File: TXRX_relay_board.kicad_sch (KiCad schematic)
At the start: 76 parts, among them J1 Screw_Terminal_01x02, J2 Conn_01x08, J3 IN, J4 IN_RF_Deck, J5 OUT_RF_Deck, J6 OUT, K1 RT314A05, K2 RT314A05, Q1 MMSS8550HE3, Q2 MMSS8550HE3, Q3 BC847, Q4 PNP, Q5 MMSS8550HE3, Q6 PNP, U1 OP07, U2 AMS1117-5.0

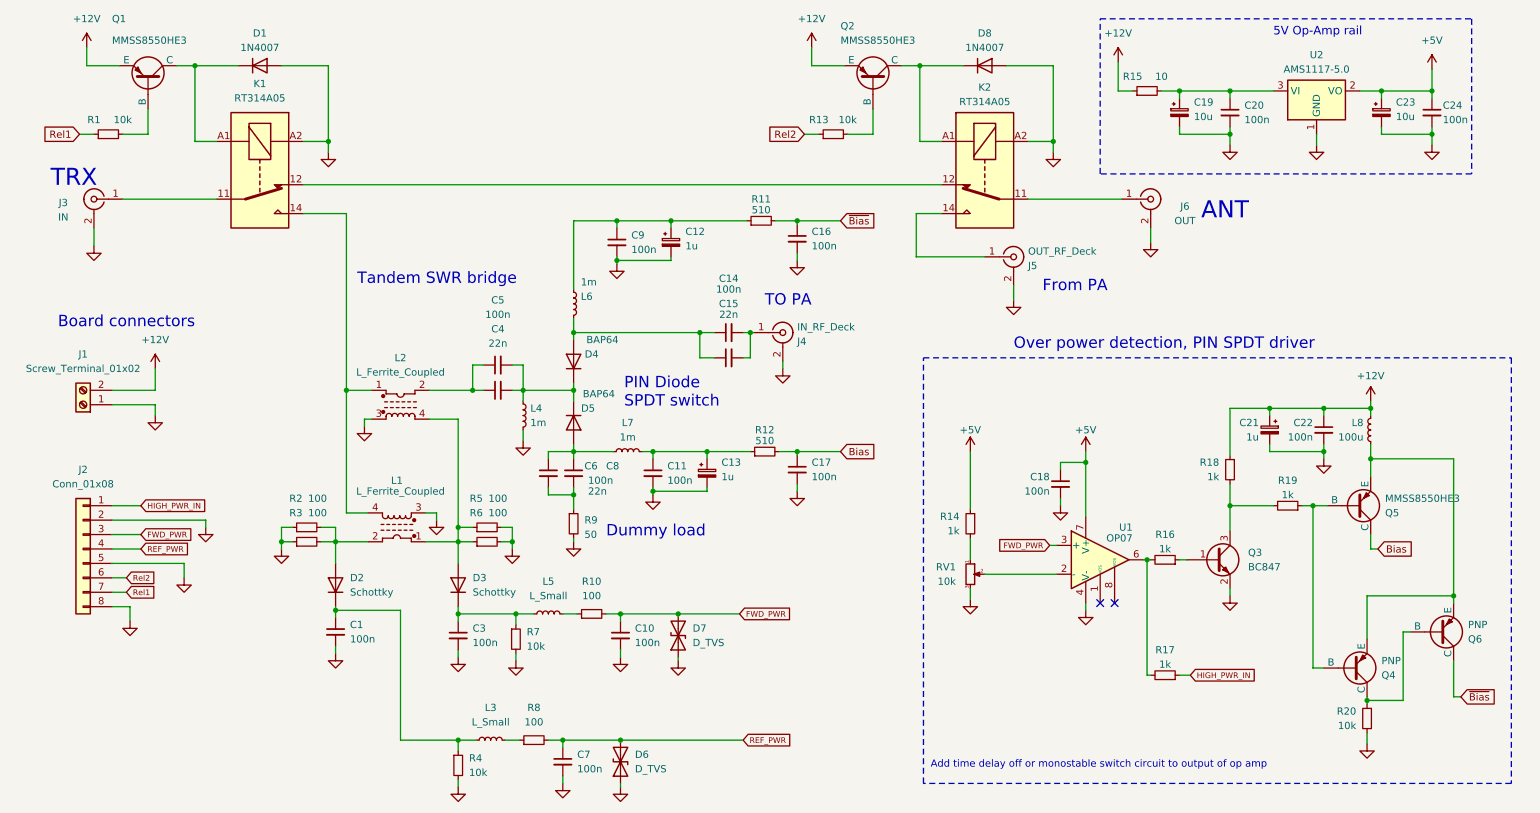
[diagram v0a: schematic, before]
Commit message: rev 1.2
Minor fixes, coupler measurements, falstad simulation of over power protection
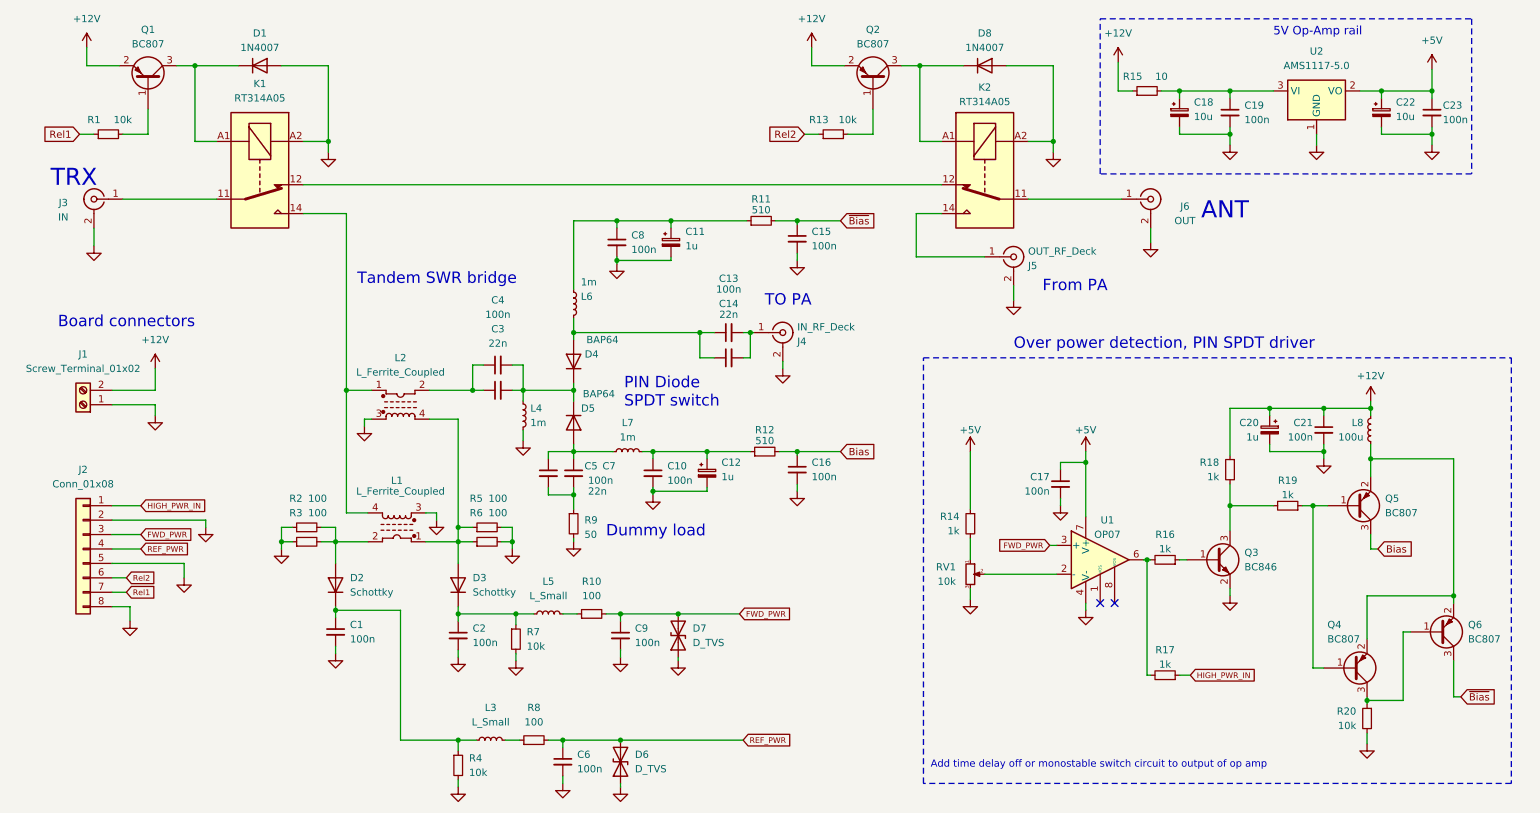
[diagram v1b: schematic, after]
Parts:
- removed Q1, Q2, Q5: MMSS8550HE3, Package_TO_SOT_SMD:SOT-23, symbol Simulation_SPICE:PNP
- removed Q3: BC847, Package_TO_SOT_SMD:SOT-23, symbol Transistor_BJT:BC847
- removed Q4, Q6: PNP, Package_TO_SOT_SMD:SOT-23, symbol Simulation_SPICE:PNP
- added Q1, Q2, Q4, Q5, Q6: BC807, Package_TO_SOT_SMD:SOT-23, symbol Transistor_BJT:BC807
- added Q3: BC846, Package_TO_SOT_SMD:SOT-23, symbol Transistor_BJT:BC846
- renumbered C11 to C10, C12 to C11, C13 to C12, C14 to C13, C15 to C14, C16 to C15, C17 to C16, C18 to C17, C19 to C18, C20 to C19, C3 to C2, C21 to C20, C22 to C21, C23 to C22, C24 to C23, C4 to C3, C5 to C4, C6 to C5, C7 to C6, C8 to C7, C9 to C8, C10 to C9
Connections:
- net +12V: now also Q1.2 (E), Q2.2 (E)
- net Bias: now also Q5.3 (C)
- net GND: now also Q3.2 (E)
- net ~{Bias}: now also Q6.3 (C)
- net at R19.1: now also Q4.1 (B), Q5.1 (B)
- net at L8.2: now also Q4.2 (E), Q5.2 (E), Q6.2 (E)
- net at R20.1: now also Q4.3 (C), Q6.1 (B)
- net at R1.2: now also Q1.1 (B)
- net at D1.1 (K), K1.A1: now also Q1.3 (C)
- net at R13.2: now also Q2.1 (B)
- net at D8.1 (K), K2.A1: now also Q2.3 (C)
- net at R18.2, R19.2: now also Q3.3 (C)
- net at R16.1: now also Q3.1 (B)

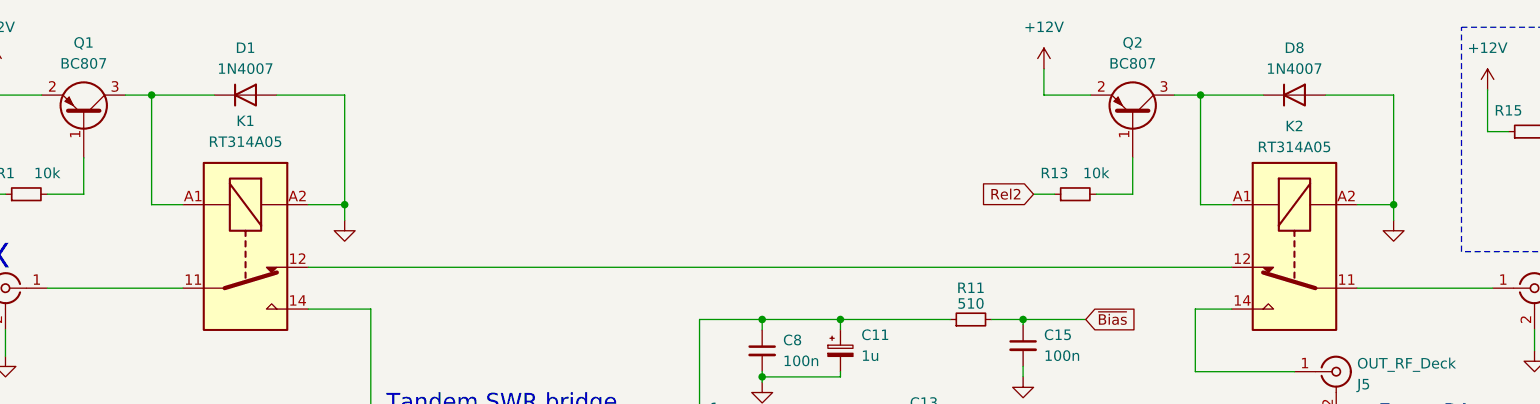
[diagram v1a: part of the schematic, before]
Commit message: Revision 1.2, fixed name of RLs, removed op amps in detector
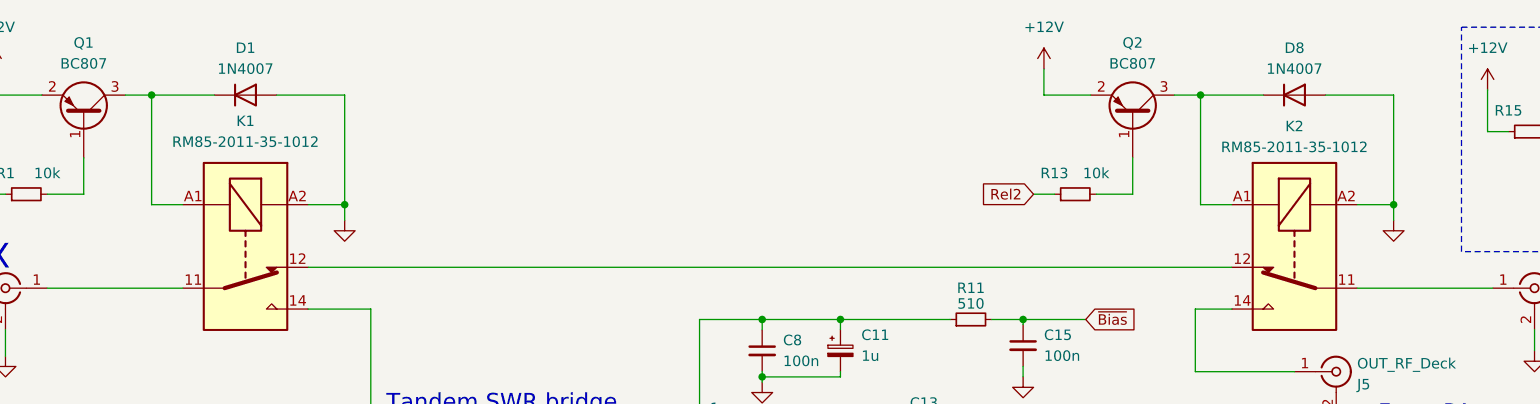
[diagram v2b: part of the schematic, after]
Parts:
- K1, K2: value RT314A05 -> RM85-2011-35-1012
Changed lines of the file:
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@@
 	(title_block
 		(title "TX-RX Relay Board")
-		(date "2024-09-05")
+		(date "2026-02-01")
 		(rev "1.2")
 		(company "SP6GK")
@@
 			)
 		)
-		(property "Value" "RT314A05"
+		(property "Value" "RM85-2011-35-1012"
 			(at 61.595 36.83 90)
 			(effects
@@
 			)
 		)
-		(property "Value" "RT314A05"
+		(property "Value" "RM85-2011-35-1012"
 			(at 189.23 37.465 90)
 			(effects
